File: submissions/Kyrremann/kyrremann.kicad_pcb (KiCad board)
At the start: 2 copper layers, 100 x 50 mm, 40 parts, among them J1 USB_C_Receptacle_USB2.0, J2 Conn_01x06_Female, J3 Conn_01x06_Female, SW1 SW_Push, U1 ATmega32U2-MU, Y1 16Mhz

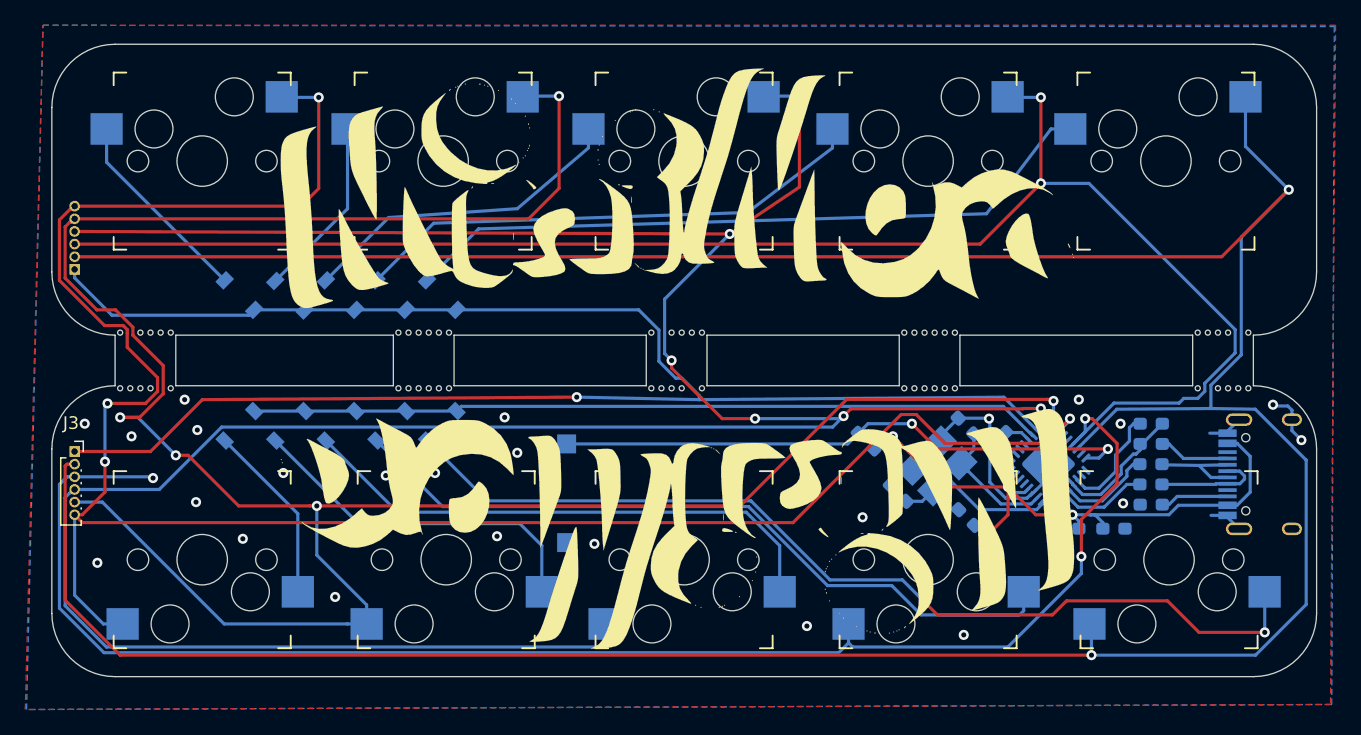
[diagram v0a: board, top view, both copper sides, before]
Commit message: Retraced the keyboard, and added cool silks
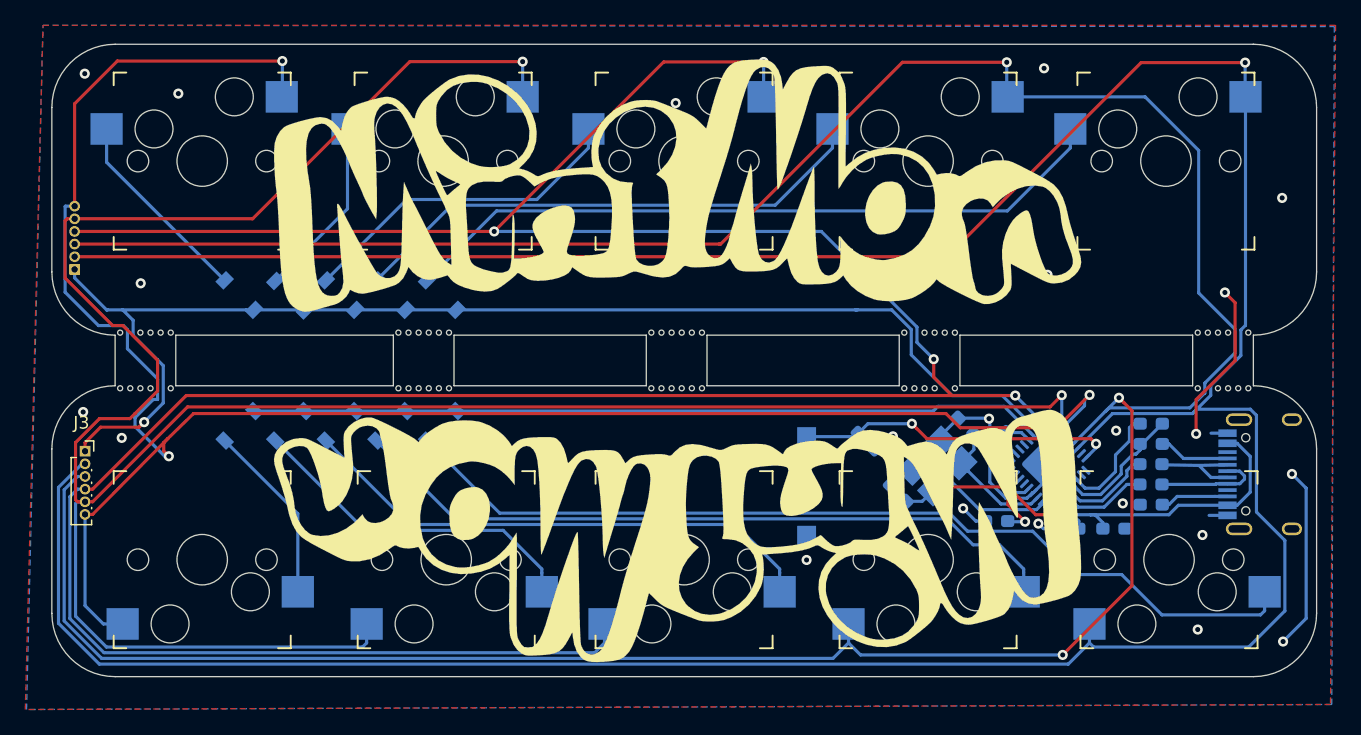
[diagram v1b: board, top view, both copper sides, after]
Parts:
- removed the G*** at (104.4, 83.3)
- removed the G*** at (104.5, 56.4)
- added G***: LOGO, keychuks:monster, B.Cu at (69.5, 82.8)
- added G***: LOGO, keychuks:logo, F.Cu at (104.5, 83.9)
- added G***: LOGO, keychuks:logo, F.Cu at (104.5, 56.2)
- moved SW1 19.0 mm to (114.7, 79.9)
- moved C4 2.40 mm to (129.7, 82.7), turned to 180 degrees
- moved J3 0.83 mm to (57.6, 77.2)
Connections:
- J1 pad S1: GND -> Net-(J1-PadS1)
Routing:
- net /ROW0: track 135.0 -> 100.1 mm
- net GND: track 42.1 -> 70.5 mm, vias 27 -> 25
- net /RESET: track 46.3 -> 25.4 mm
- net /COL02: track 232.6 -> 242.2 mm, vias 6 -> 4
- net /COL01: track 247.4 -> 252.4 mm, vias 5 -> 3
- net /COL04: track 160.8 -> 156.3 mm, vias 4 -> 3
- net Net-(D6-Pad2): track 76.6 -> 73.6 mm, vias 2 -> 0
- net Net-(D7-Pad2): track 58.5 -> 57.2 mm
- net /+5v: track 53.2 -> 51.9 mm
- net /COL03: track 192.5 -> 193.6 mm, vias 5 -> 2
- net Net-(D9-Pad2): track 28.2 -> 27.1 mm
- net Net-(D8-Pad2): track 43.0 -> 41.9 mm
- net /COL00: track 274.9 -> 275.7 mm, vias 2 -> 1
- net Net-(D1-Pad2): track 55.9 -> 56.7 mm
- net Net-(D2-Pad2): track 41.9 -> 42.4 mm
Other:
- outline, holes or cut-outs redrawn
